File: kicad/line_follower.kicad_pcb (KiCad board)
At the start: 2 copper layers, 80 x 100 mm, 48 parts, among them J1 XT30PW-M, M1 MOTOR_ENC, M2 MOTOR_ENC, Q1 ALS-PT19-315C_L177_TR8, Q2 ALS-PT19-315C_L177_TR8, Q3 ALS-PT19-315C_L177_TR8, Q4 ALS-PT19-315C_L177_TR8, Q5 ALS-PT19-315C_L177_TR8, SW1 SW_Push, U1 A4950E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

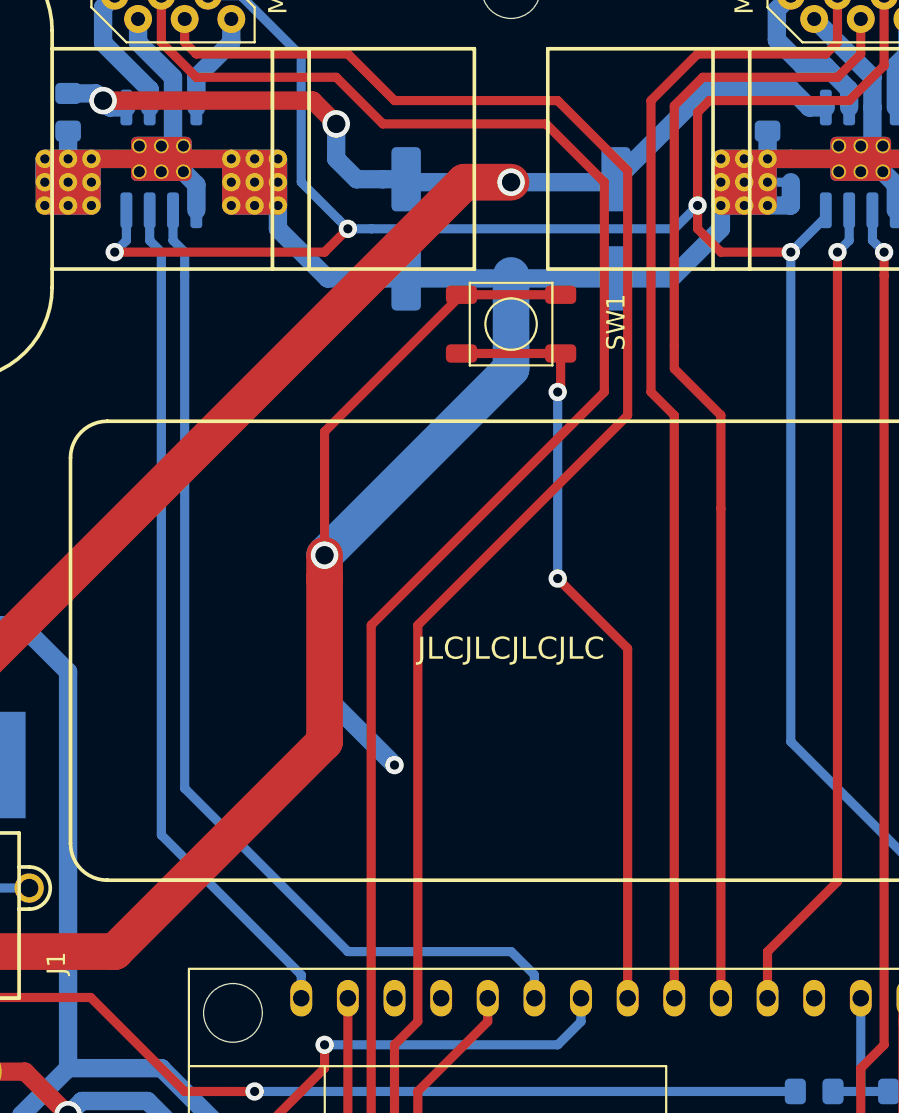
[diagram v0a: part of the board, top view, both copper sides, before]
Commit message: board: Small tweaks + updating to match previous changes.
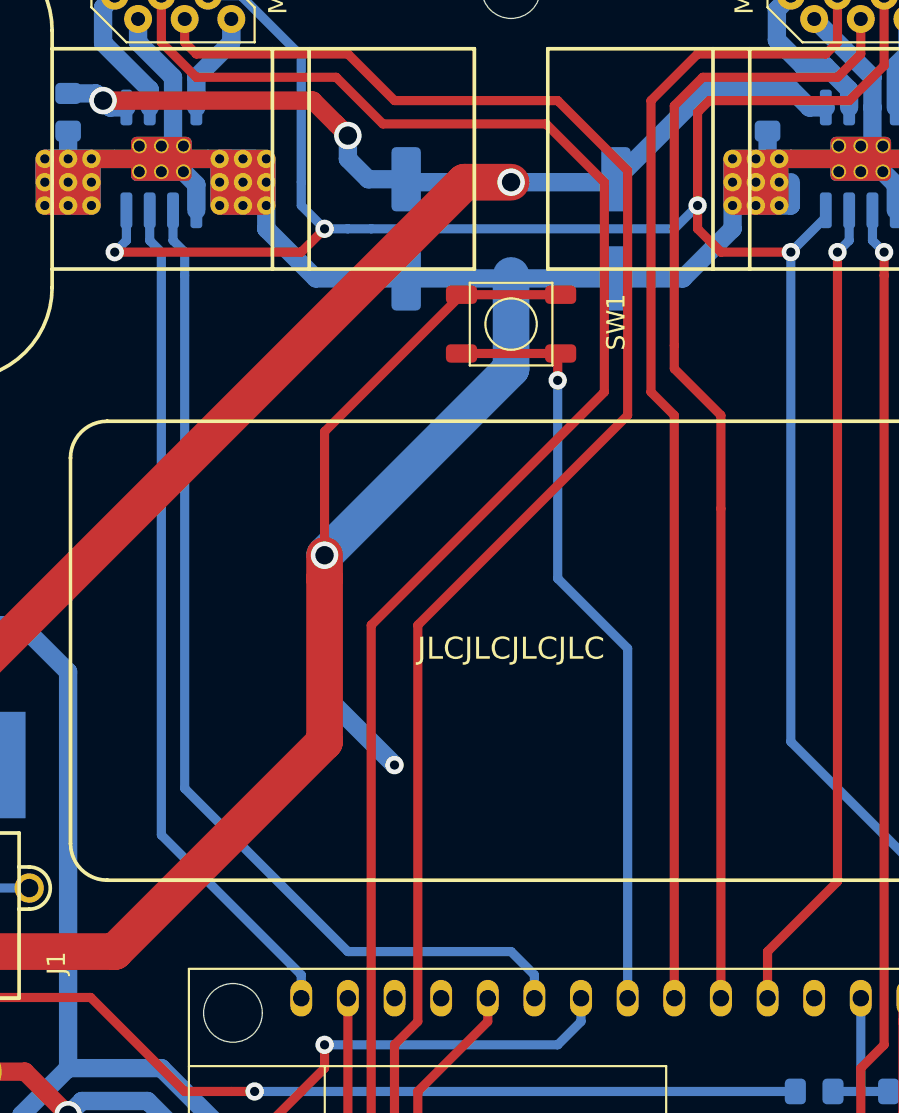
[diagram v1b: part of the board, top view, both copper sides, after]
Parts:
- moved HS2 0.64 mm to (13.3, 1.27)
- moved HS4 0.63 mm to (-14.6, 1.27)
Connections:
- net LINE_LED0 renamed /LINE_LED0
- net LINE_LED1 renamed /LINE_LED1
- net LINE_LED2 renamed /LINE_LED2
- net LINE_SENSOR0 renamed /LINE_SENSOR0
- net LINE_SENSOR1 renamed /LINE_SENSOR1
- net LINE_SENSOR2 renamed /LINE_SENSOR2
- net LINE_SENSOR3 renamed /LINE_SENSOR3
- net LINE_SENSOR4 renamed /LINE_SENSOR4
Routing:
- net GND: track 433.6 -> 424.7 mm
- net +3V3: track 213.8 -> 213.3 mm
- net /BUTTON: vias 2 -> 1

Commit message: schematic: Changed the 5V regulator again
the previous one had wrong pinout
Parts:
- U3: value NCV4274CDT50RKG -> LF50CDT
